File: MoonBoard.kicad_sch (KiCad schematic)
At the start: 28 parts, among them J1 USB_A, J2 USB_A, J3 USB_A, SW1 SW_SPST, U1 AMS1117-3.3, U10 SL2.1A, U2 STM32F446RETx, Y1 25MHz

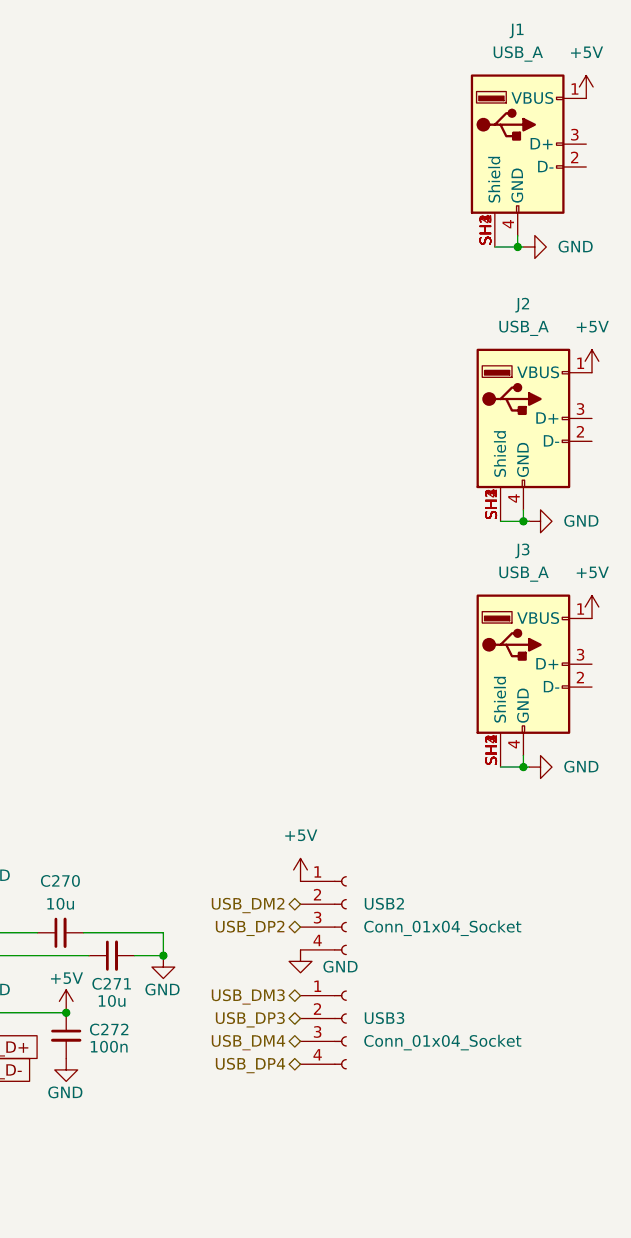
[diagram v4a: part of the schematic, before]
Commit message: make room for usb connectors
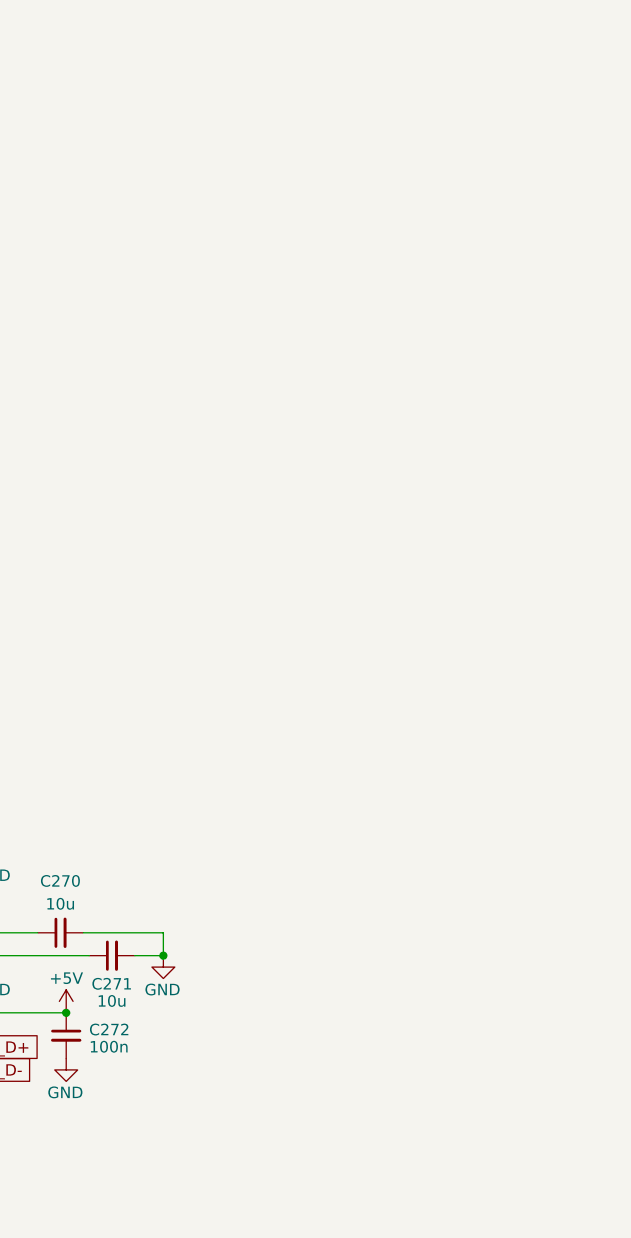
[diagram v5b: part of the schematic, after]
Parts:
- removed J1, J2, J3: USB_A, MoonBoard:USB-A-SMD_AF-APPLE-10.6, symbol Connector:USB_A
- removed USB2, USB3: Conn_01x04_Socket, Connector_Molex:Molex_Pico-EZmate_78171-0004_1x04-1MP_P1.20mm_Vertical, symbol Connector:Conn_01x04_Socket

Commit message: finish routing
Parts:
- removed C270, C271: 10u, symbol Device:C_Small
- removed C272: 100n, Capacitor_SMD:C_0402_1005Metric, symbol Device:C_Small
- removed U10: SL2.1A, MoonBoard:SSOP-16_L4.6-W2.6-P0.53-LS4.0-BL, symbol MoonBoard:SL2.1A
- removed USB1: Conn_01x04_Socket, Connector_Molex:Molex_Pico-EZmate_78171-0004_1x04-1MP_P1.20mm_Vertical, symbol Connector:Conn_01x04_Socket
- added ENCODER1: EC11E, PCM_marbastlib-various:ROT_Alps_EC11E-Switch, symbol Device:RotaryEncoder_Switch
- added OLED1: Conn_01x04_Socket, MoonBoard:OLED Module, symbol Connector:Conn_01x04_Socket
- added USB1: PicoEZMate, MoonBoard:PicoEZMate-Reinforced-Alt, symbol Connector_Generic:Conn_01x04
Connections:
- net +5V: now also OLED1.2 (Pin_2), USB1.1 (Pin_1)
- net ENCODER_A: now also ENCODER1.A
- net ENCODER_B: now also ENCODER1.B
- net GND: now also ENCODER1.C, ENCODER1.S1, OLED1.1 (Pin_1), USB1.4 (Pin_4)
- net I2C1_SCL: now also OLED1.3 (Pin_3)
- net I2C1_SDA: now also OLED1.4 (Pin_4)
- net ENCODER_SW: now reaches U2.3 (PC14)
- net ENCODER_SW: now also ENCODER1.S2
- net ADC123_IN10: no longer names the net of U2.8 (PC0)
- net ADC123_IN11: no longer names the net of U2.9 (PC1)
- net MUX_S0 renamed S0
- net MUX_S1 renamed S1
- net MUX_S2 renamed S2
- net MUX_S3 renamed S3
- net NRESET renamed ~{RESET}
- net USB_DM1 renamed D-
- net D-: now also USB1.2 (Pin_2)
- net USB_DP1 renamed D+
- net D+: now also USB1.3 (Pin_3)

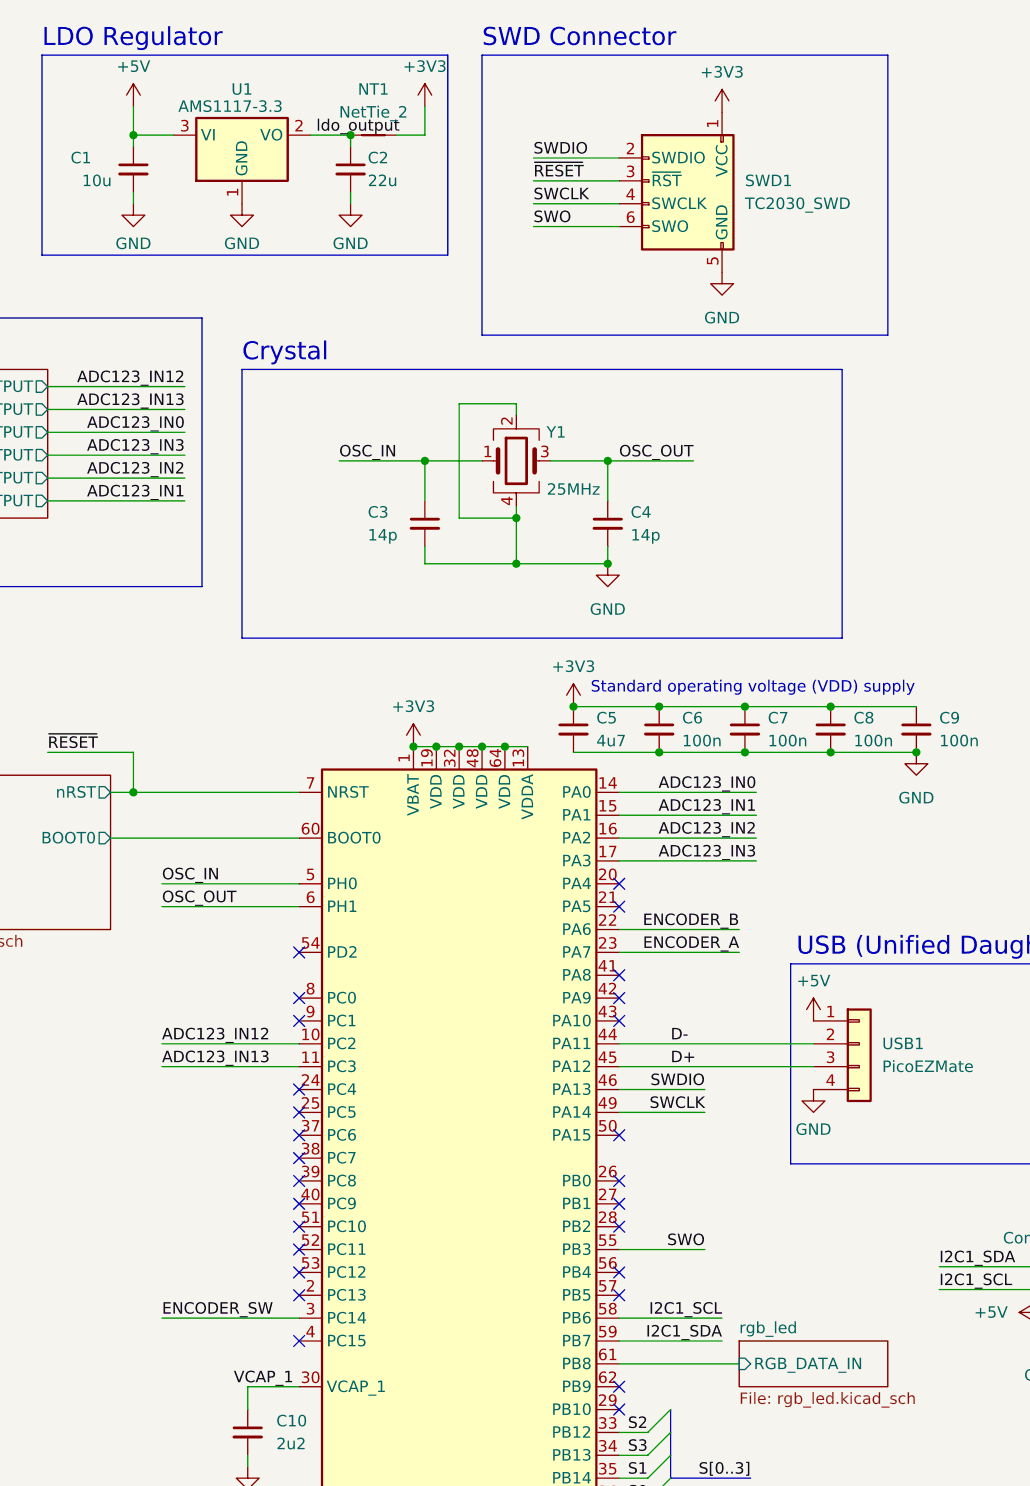
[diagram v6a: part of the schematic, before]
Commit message: switch to SOIC multiplexers
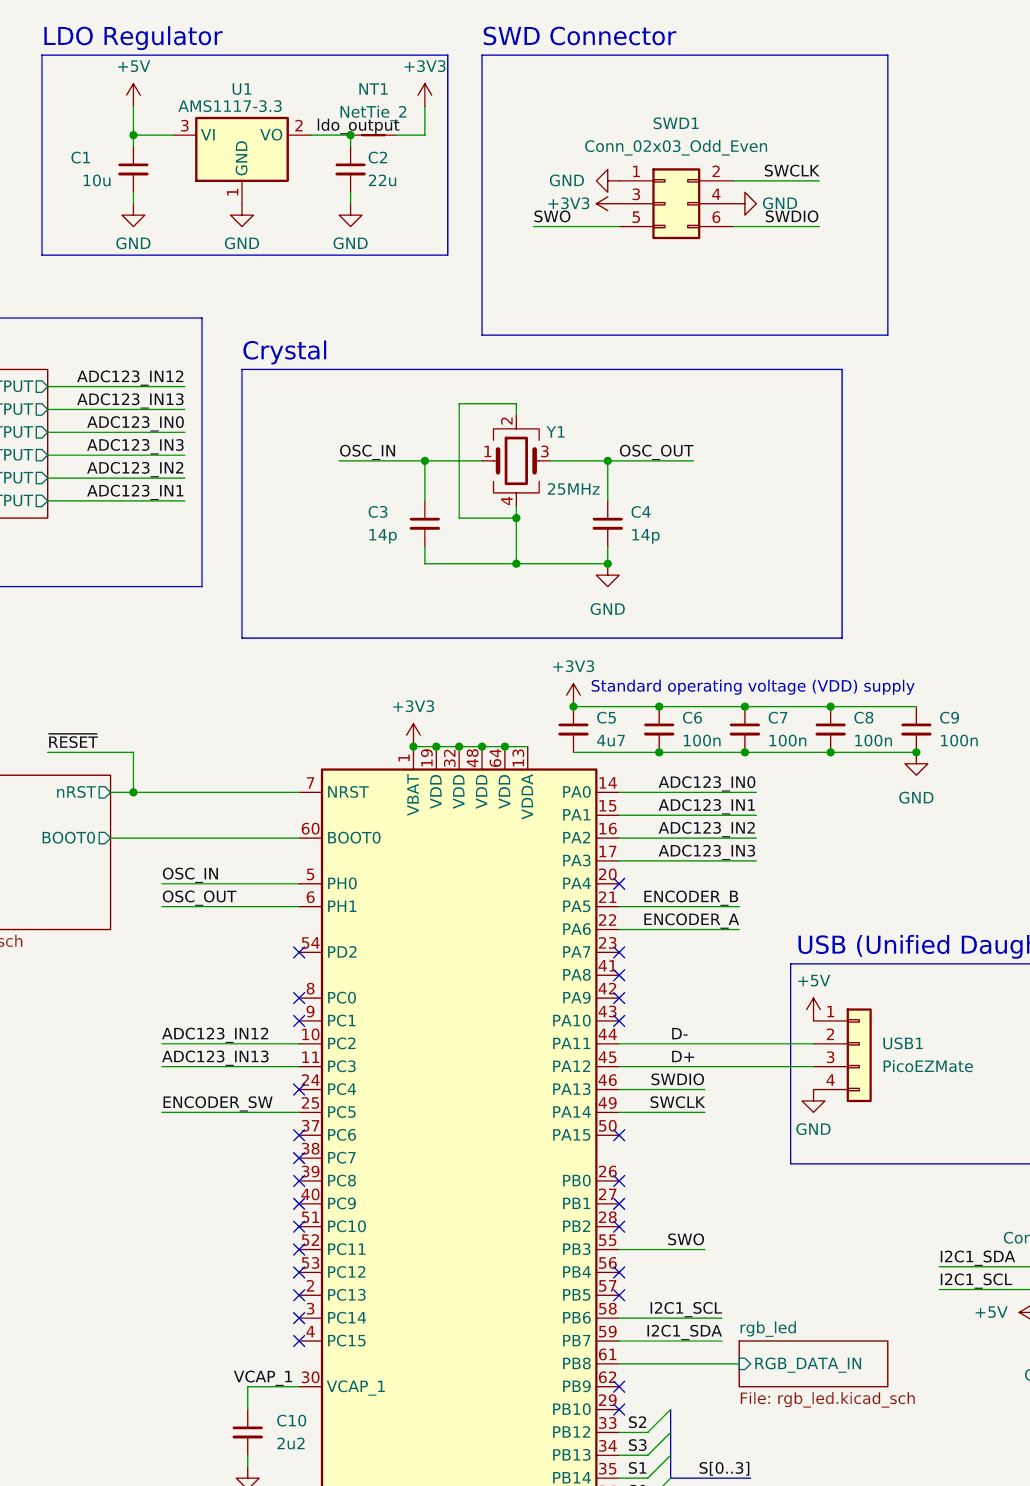
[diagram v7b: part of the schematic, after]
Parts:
- removed SWD1: TC2030_SWD, PCM_marbastlib-various:CON_TC2030_outlined, symbol PCM_marbastlib-various:TC2030_SWD
- added SWD1: Conn_02x03_Odd_Even, Connector_PinHeader_2.54mm:PinHeader_2x03_P2.54mm_Vertical, symbol Connector_Generic:Conn_02x03_Odd_Even
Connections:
- net +3V3: now also SWD1.3 (Pin_3)
- net ENCODER_A: now also U2.22 (PA6); no longer U2.23 (PA7)
- net ENCODER_B: now also U2.21 (PA5); no longer U2.22 (PA6)
- net ENCODER_SW: now also U2.25 (PC5); no longer U2.3 (PC14)
- net GND: now also SWD1.1 (Pin_1), SWD1.4 (Pin_4)
- net SWCLK: now also SWD1.2 (Pin_2)
- net SWDIO: now also SWD1.6 (Pin_6)
- net SWO: now also SWD1.5 (Pin_5)

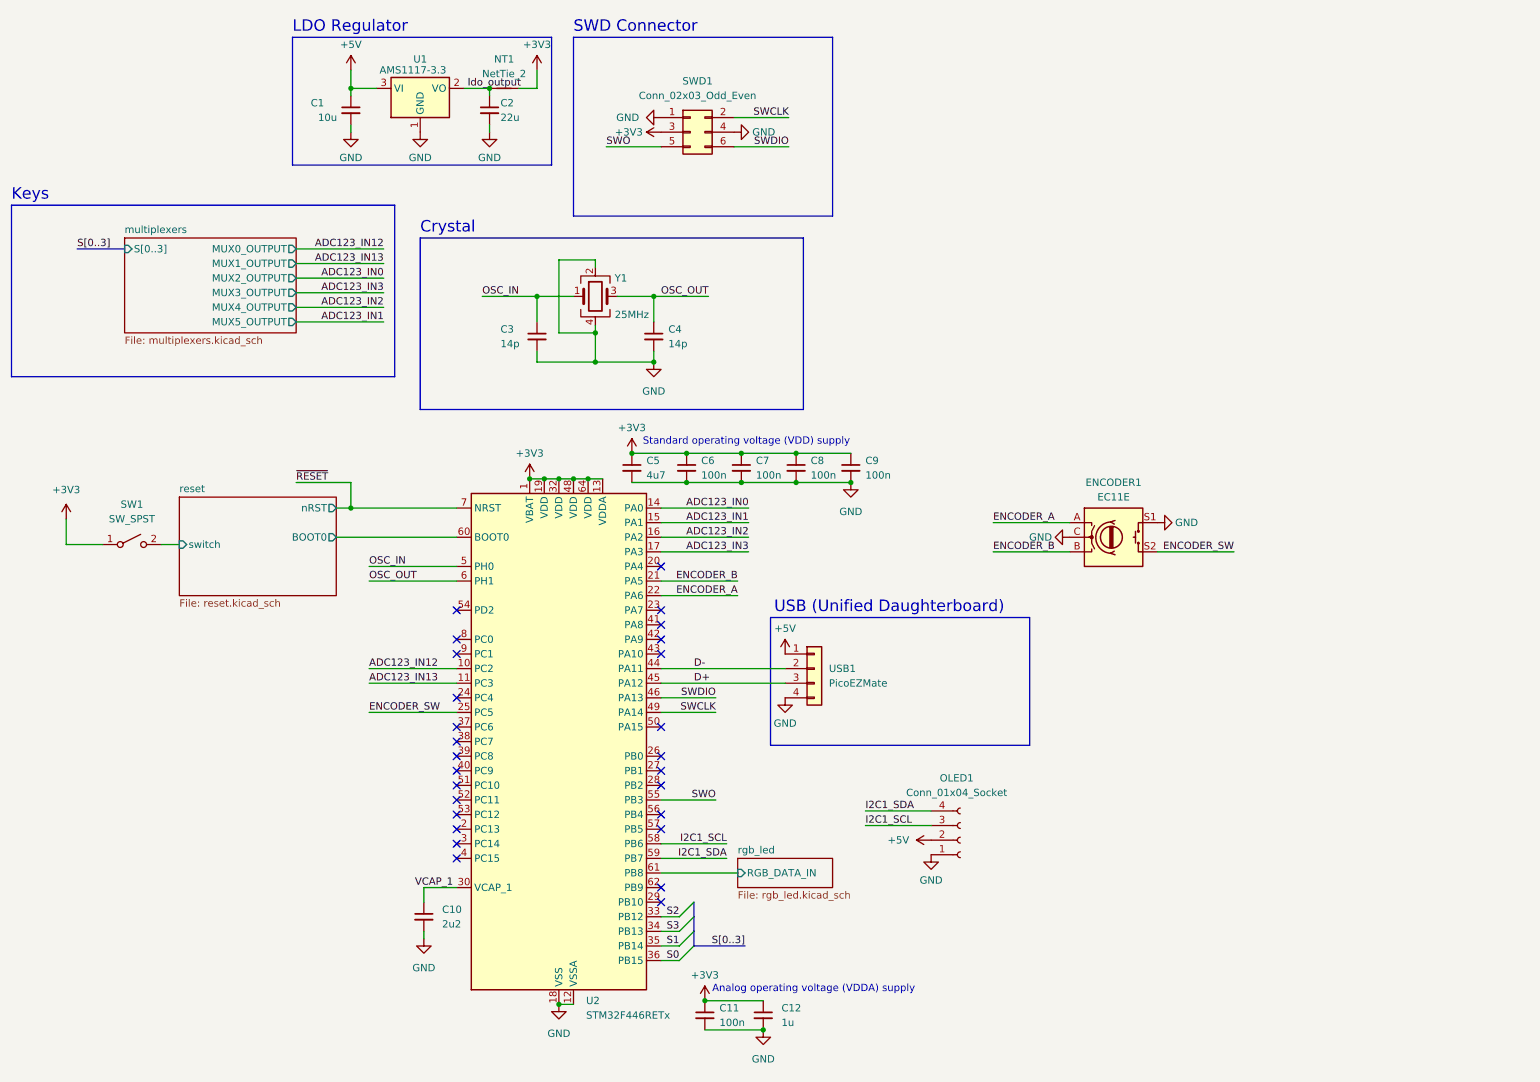
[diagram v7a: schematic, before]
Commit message: add level shifter for rgb data line
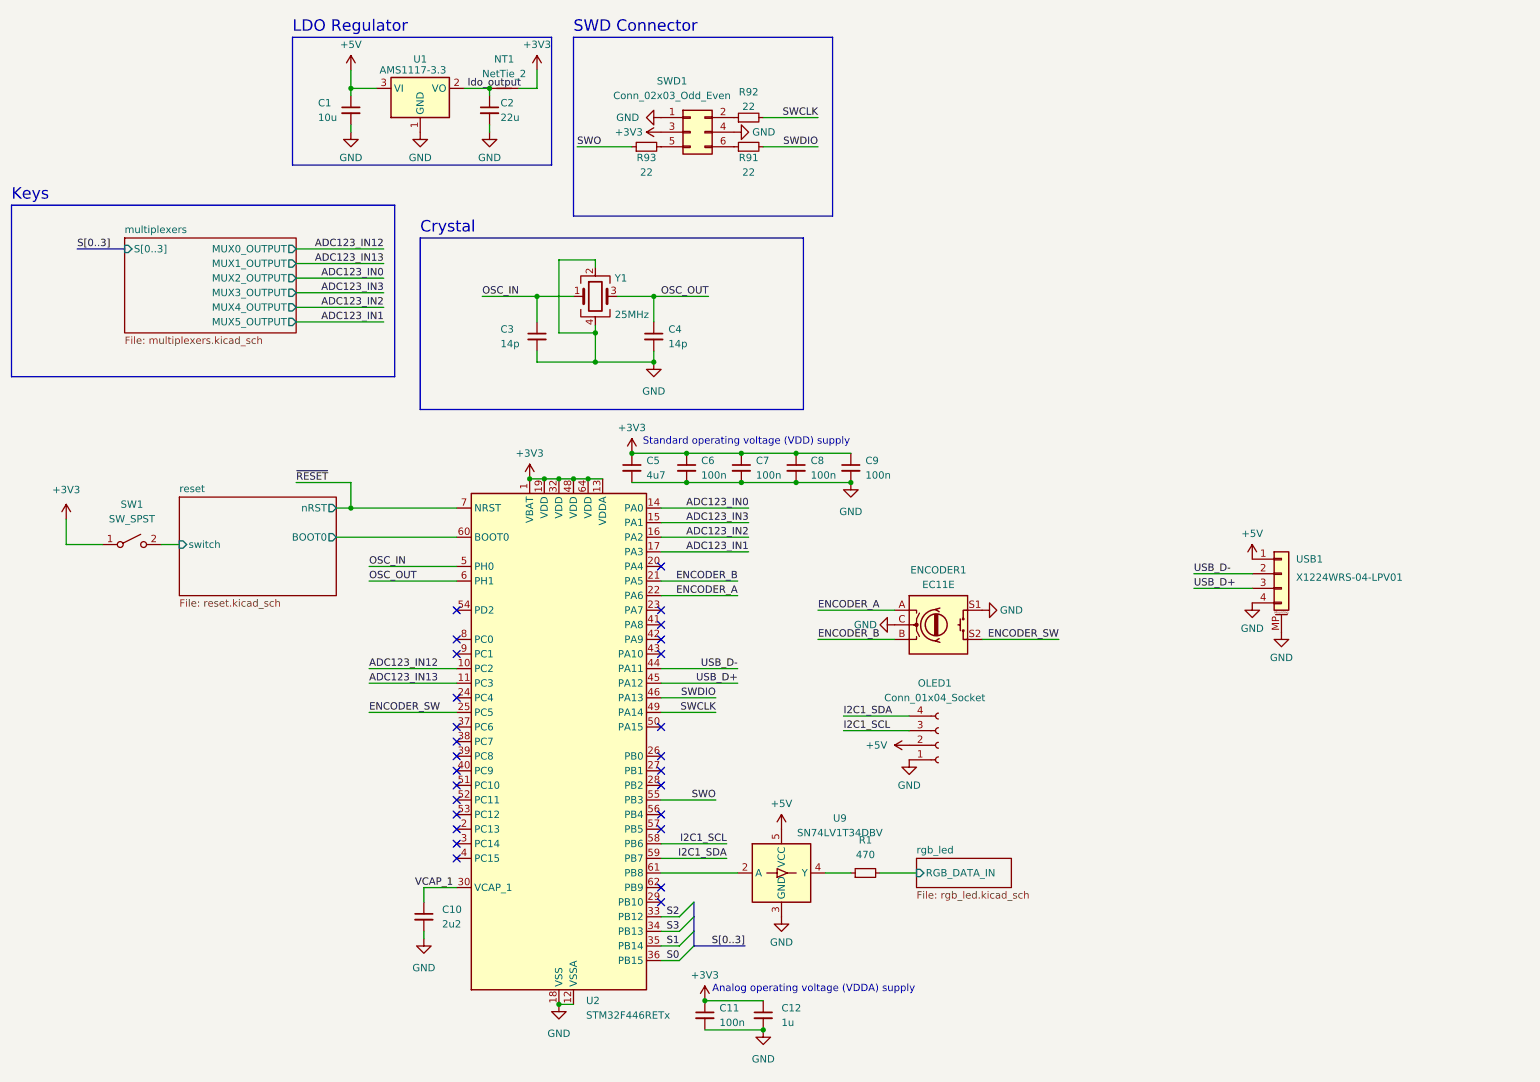
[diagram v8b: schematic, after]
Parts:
- removed USB1: PicoEZMate, MoonBoard:PicoEZMate-Reinforced-Alt, symbol Connector_Generic:Conn_01x04
- added R1: 470, Resistor_SMD:R_0402_1005Metric, symbol Device:R_Small
- added R91, R92, R93: 22, Resistor_SMD:R_0402_1005Metric, symbol Device:R_Small
- added U9: SN74LV1T34DBV, Package_TO_SOT_SMD:SOT-23-5, symbol Logic_LevelTranslator:SN74LV1T34DBV
- added USB1: X1224WRS-04-LPV01, MoonBoard:PicoEZMate-Reinforced-Alt, symbol Connector_Generic_MountingPin:Conn_01x04_MountingPin
- C1, C2: footprint Capacitor_Tantalum_SMD:CP_EIA-3216-18_Kemet-A -> Capacitor_SMD:C_1206_3216Metric
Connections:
- net +5V: now also U9.5 (VCC), USB1.1 (Pin_1)
- net ADC123_IN1: now also U2.17 (PA3); no longer U2.15 (PA1)
- net ADC123_IN3: now also U2.15 (PA1); no longer U2.17 (PA3)
- net GND: now also U9.3 (GND), USB1.4 (Pin_4), USB1.MP (MountPin)
- net SWCLK: now also R92.2; no longer SWD1.2 (Pin_2)
- net SWDIO: now also R91.2; no longer SWD1.6 (Pin_6)
- net SWO: now also R93.1; no longer SWD1.5 (Pin_5)
- net rgb_led/RGB_DATA_IN: now also R1.2; no longer U2.61 (PB8)
- net D+ renamed USB_D+
- net USB_D+: now also USB1.3 (Pin_3)
- net D- renamed USB_D-
- net USB_D-: now also USB1.2 (Pin_2)
- new net: R92.1, SWD1.2 (Pin_2)
- new net: R93.2, SWD1.5 (Pin_5)
- new net: R91.1, SWD1.6 (Pin_6)
- new net: U2.61 (PB8), U9.2 (A)
- new net: R1.1, U9.4 (Y)
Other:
- note removed: "USB (Unified Daughterboard)"
- moved on the sheet: ENCODER1, OLED1
